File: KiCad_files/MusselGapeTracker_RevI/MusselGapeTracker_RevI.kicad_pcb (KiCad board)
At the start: 2 copper layers, 72.5 x 57.8 mm, 83 parts, among them J1 AVR_SPI_PRG_6PTH, U1 ATMEGA328P, U2 DS3231M+TRL, U3 DS3231MZ

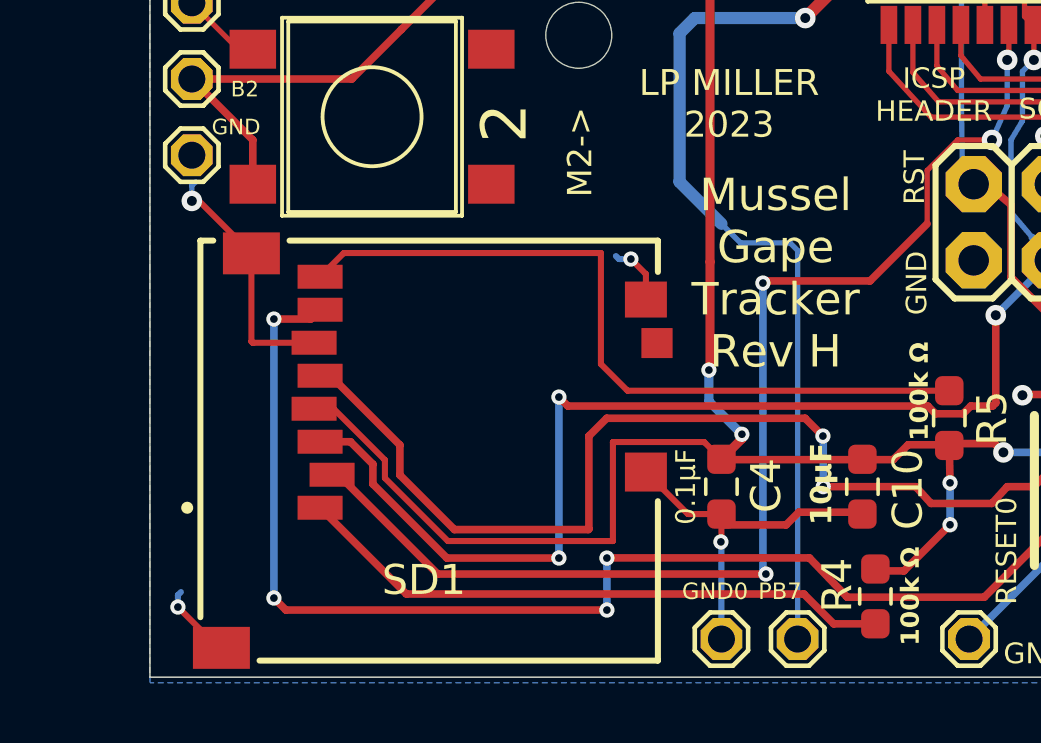
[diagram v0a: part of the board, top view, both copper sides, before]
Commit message: Moved changes to Rev I and fixed DRC errors
Made new copy of KiCad project in Rev I and fixed some electric rules checker errors and warnings and some design rules checker errors and warnings
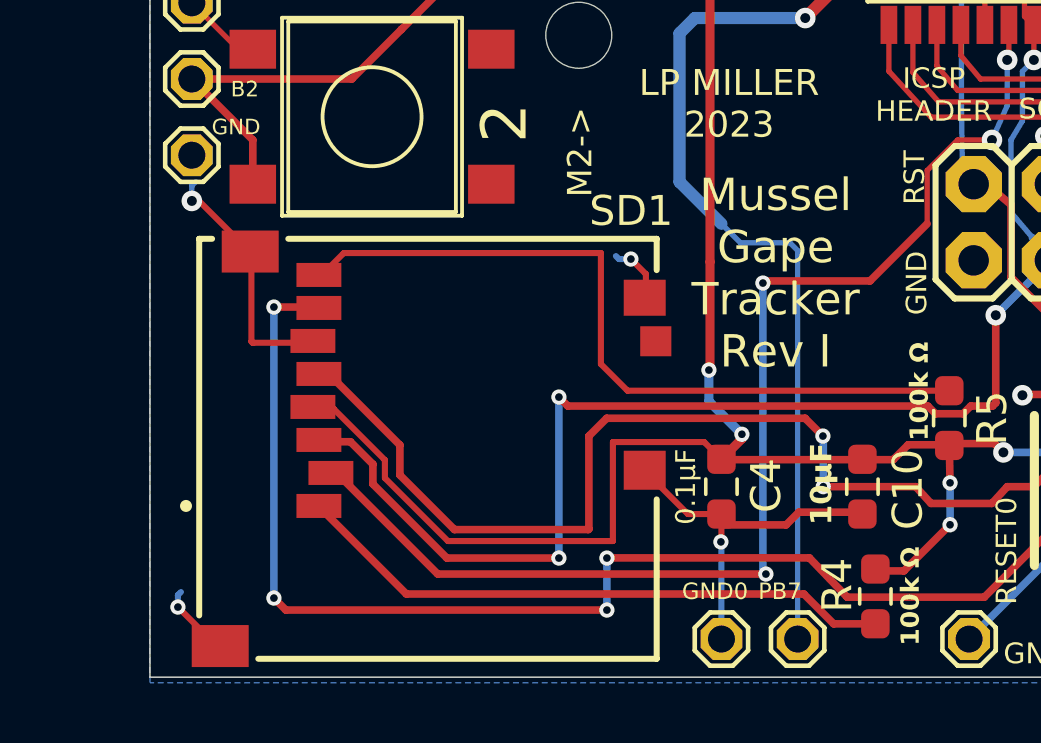
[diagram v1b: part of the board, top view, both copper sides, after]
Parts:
- BJT0: footprint MusselGapeTracker_RevE:SOT23 -> MusselGapeTracker_RevI:SOT23
- BUTTON1, BUTTON2: footprint MusselGapeTracker_RevE:PUSHBUTTON_DPST_SMD -> MusselGapeTracker_RevI:PUSHBUTTON_DPST_SMD
- C1, C2: footprint MusselGapeTracker_RevE:PANASONIC_B -> MusselGapeTracker_RevI:PANASONIC_B
- CR1220_BATTERY0: footprint MusselGapeTracker_RevE:CR1220_BATTERY_HOLDER_SMD -> MusselGapeTracker_RevI:CR1220_BATTERY_HOLDER_SMD
- GND0, PB7, U$10, U$11, U$17, U$3, U$4, U$6, U$7, U$8, U$9: footprint MusselGapeTracker_RevE:1X01_SMALL -> MusselGapeTracker_RevI:1X01_SMALL
- GROUND_CON0: footprint MusselGapeTracker_RevE:SJ_2S-TRACE -> MusselGapeTracker_RevI:SJ_2S-TRACE
- HALL0, HALL1, HALL10, HALL11, HALL12, HALL13, HALL14, HALL15, HALL2, HALL3, HALL4, HALL5, HALL6, HALL7, HALL8, HALL9: footprint MusselGapeTracker_RevE:JST-PH-4-THM -> MusselGapeTracker_RevI:JST-PH-4-THM
- INDUCTOR0: footprint MusselGapeTracker_RevE:I_0805 -> MusselGapeTracker_RevI:I_0805
- J1: footprint MusselGapeTracker_RevE:2X3 -> MusselGapeTracker_RevI:2X3
- JP1: footprint MusselGapeTracker_RevE:1X06-RIGHT_ANGLE -> MusselGapeTracker_RevI:1X06-RIGHT_ANGLE
- LED1, LED2: footprint MusselGapeTracker_RevE:CHIPLED_0805 -> MusselGapeTracker_RevI:CHIPLED_0805
- MCP1700T-3302: footprint MusselGapeTracker_RevE:SOT95P237X112-3N -> MusselGapeTracker_RevI:SOT95P237X112-3N
- MOLEX_KK0: footprint MusselGapeTracker_RevE:22-23-2021 -> MusselGapeTracker_RevI:22-23-2021
- OLED0: footprint MusselGapeTracker_RevE:1X04_LOCK -> MusselGapeTracker_RevI:1X04_LOCK
- PFET-0: footprint MusselGapeTracker_RevH:SOT23-3 -> MusselGapeTracker_RevI:SOT23-3
- RESET0: footprint MusselGapeTracker_RevE:PUSHBUTTON_SPST_PTS525_SERIES -> MusselGapeTracker_RevI:PUSHBUTTON_SPST_PTS525_SERIES
- SD1: value GCT_MEM2052-00-195-00-A_REVA -> MEM2052-00-195-00-A_REVA; footprint MusselGapeTracker_RevH:GCT_MEM2052-00-195-00-A_REVA -> MusselGapeTracker_RevI:GCT_MEM2052-00-195-00-A_REVA
- SHIFT_0, SHIFT_1: footprint MusselGapeTracker_RevE:SO16 -> MusselGapeTracker_RevI:SO16
- STANDOFF1, STANDOFF2, STANDOFF3: footprint MusselGapeTracker_RevE:STAND-OFF -> MusselGapeTracker_RevI:STAND-OFF
- STANDOFF4_M2, STANDOFF5_M2: footprint MusselGapeTracker_RevE:STAND-OFF_M2 -> MusselGapeTracker_RevI:STAND-OFF_M2
- U1: footprint MusselGapeTracker_RevE:TQFP32-08 -> MusselGapeTracker_RevI:TQFP32-08
- UNK2,1MM_JACK0: footprint MusselGapeTracker_RevE:POWER_JACK_DC_2,1MM -> MusselGapeTracker_RevI:POWER_JACK_DC_2,1MM
- moved SD1 0.07 mm to (107.2, 126.3)
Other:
- board text added: "Mussel Gape Tracker Rev I"
